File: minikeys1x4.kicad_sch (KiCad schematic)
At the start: 15 parts

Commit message: add placeholder keys, xtals, LED, debug
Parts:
- added C? (x2): DNP, symbol Device:C_Small
- added C? (x2): ?, symbol Device:C_Small
- added D?: LED_Small, symbol Device:LED_Small
- added R? (x2): ?, symbol Device:R_Small_US
- added R?: 0, symbol Device:R_Small_US
- added SW? (x4): SW_Push_45deg, symbol Switch:SW_Push_45deg
- added Y?: 32kHz, symbol Device:Crystal_GND24_Small
- added Y?: 8MHz, symbol Device:Crystal_GND24_Small
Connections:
- net +3V3: now also SW?.1, SW?.1, SW?.1, SW?.1
- net GND: now also C?.2, C?.2, C?.2, C?.2, R?.2, Y?.2 (G), Y?.2 (G), Y?.4 (G), Y?.4 (G)
- net nRST: now also C?.1; no longer R?.2, SW?.1
- net KEY_0: now reaches U?.11 (PA1)
- net KEY_0: now also SW?.2
- net KEY_1: now reaches U?.12 (PA2)
- net KEY_1: now also SW?.2
- net KEY_2: now reaches U?.13 (PA3)
- net KEY_2: now also SW?.2
- net KEY_3: now reaches U?.14 (PA4)
- net KEY_3: now also SW?.2
- net LED_0: now reaches U?.16 (PA6)
- net LED_0: now also D?.2 (A)
- net LSE_IN: now reaches U?.3 (PC14)
- net LSE_IN: now also C?.1, Y?.3
- net USBD_N: now reaches U?.32 (PA11)
- net USBD_P: now reaches U?.33 (PA12)
- net SWDIO: now reaches U?.34 (PA13)
- net SWCLK: now reaches U?.37 (PA14)
- net JTDI: now reaches U?.38 (PA15)
- net JTDO: now reaches U?.39 (PB3)
- net LSE_OUT: now reaches U?.4 (PC15)
- net LSE_OUT: now also R?.1
- net NJTRST: now reaches U?.40 (PB4)
- net HSE_IN: now reaches U?.5 (PD0)
- net HSE_IN: now also C?.1, Y?.3
- net HSE_OUT: now reaches U?.6 (PD1)
- net HSE_OUT: now also R?.1
- new net: R?.2, SW?.1
- new net: C?.1, R?.2, Y?.1 (x2)
- new net: D?.1 (K), R?.1
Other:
- note added: "TIM3_CH1"
- note added: "should this LED low side drive?"
- moved on the sheet: C?, J?, R?, SW?, U?

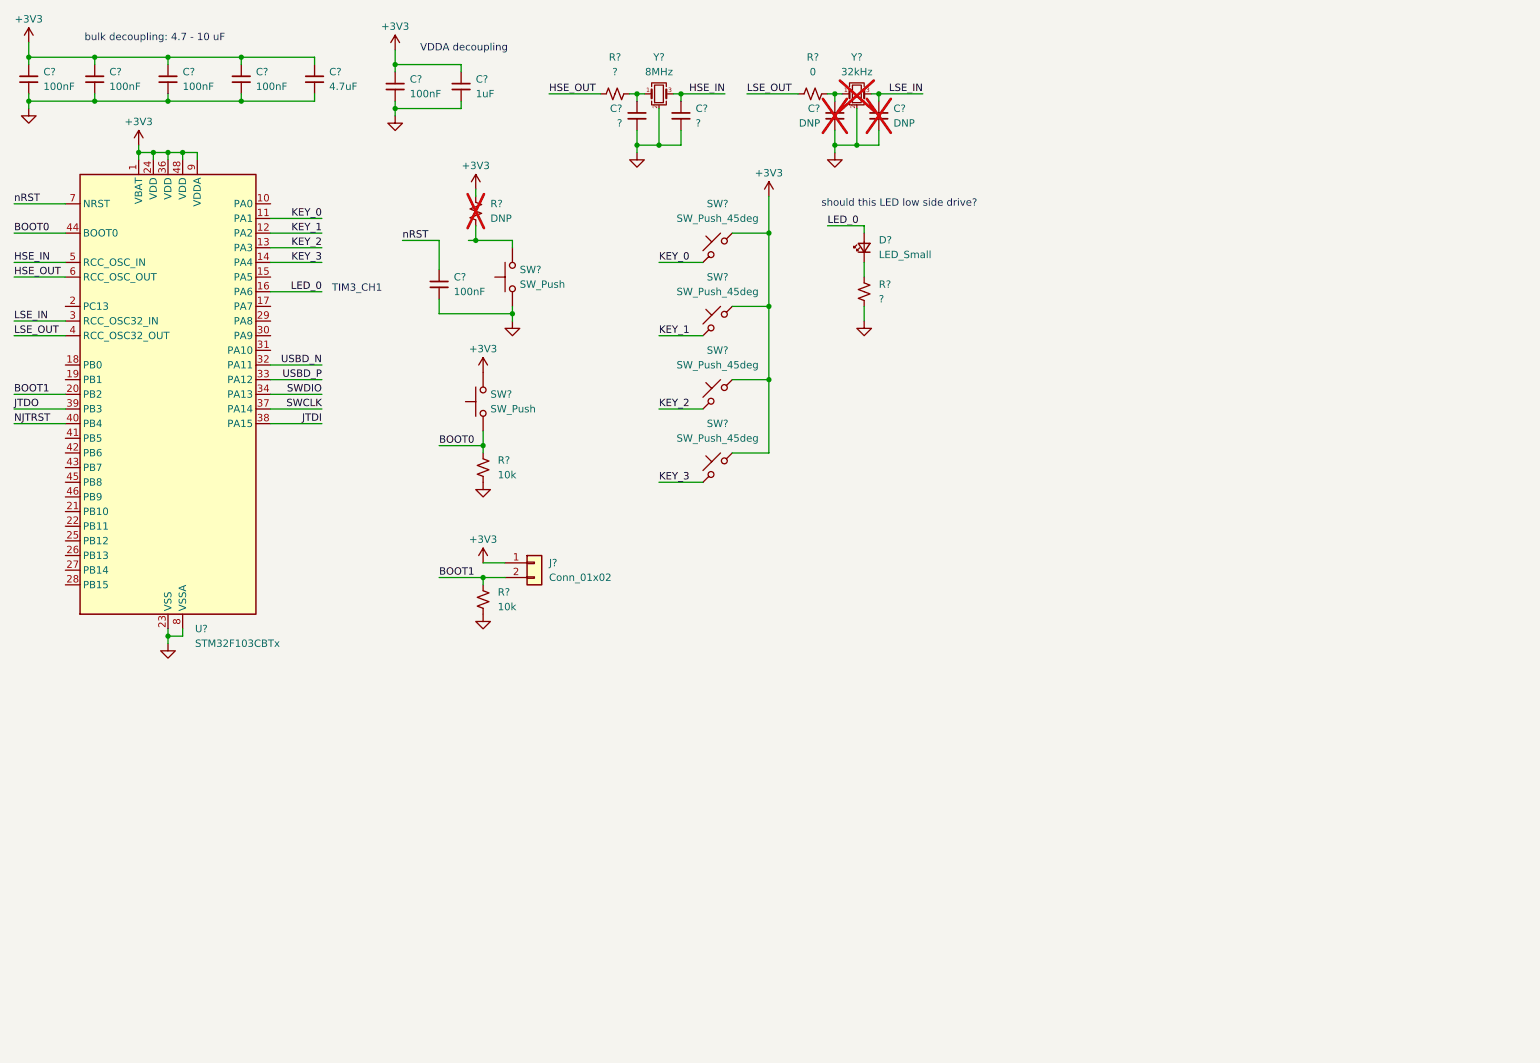
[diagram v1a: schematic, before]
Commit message: add project footprint and USB
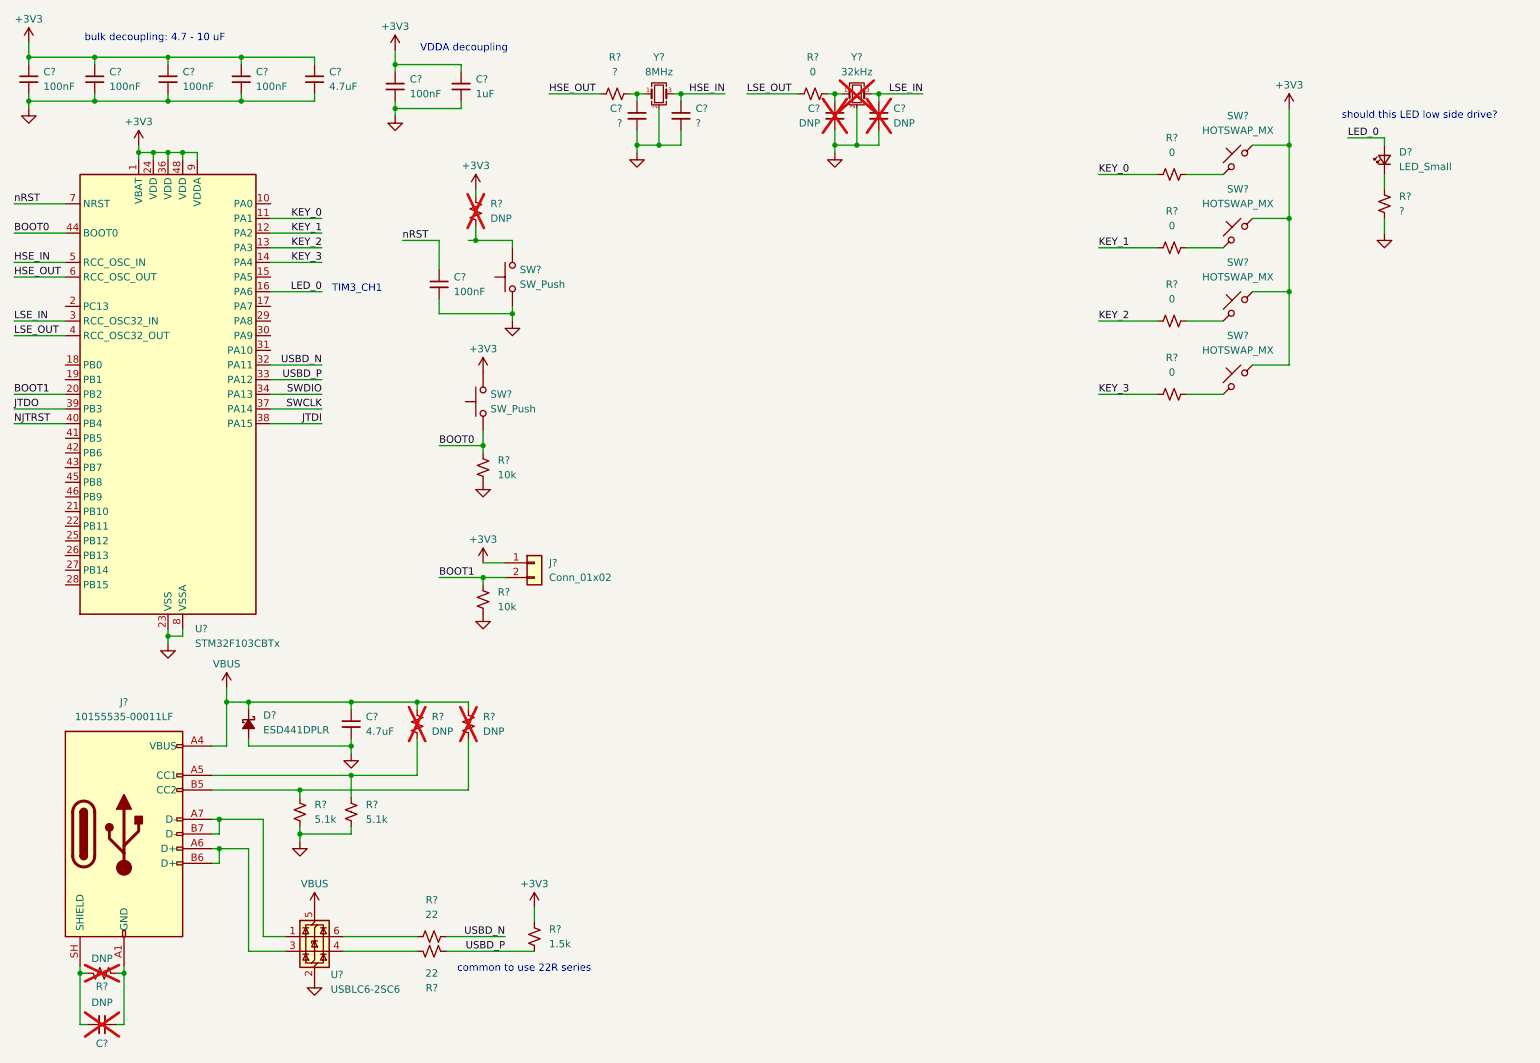
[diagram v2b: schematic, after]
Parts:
- added C?: DNP, symbol Device:C_Small
- added C?: 4.7uF, symbol Device:C_Small
- added D?: ESD441DPLR, symbol Device:D_Schottky_Small_Filled
- added J?: 10155535-00011LF, symbol Connector:USB_C_Receptacle_USB2.0_14P
- added R?: 1.5k, symbol Device:R_Small_US
- added R? (x2): 22, symbol Device:R_Small_US
- added R? (x3): DNP, symbol Device:R_Small_US
- added R? (x2): 5.1k, symbol Device:R_Small_US
- added R? (x4): 0, symbol Device:R_Small_US
- added U?: USBLC6-2SC6, Package_TO_SOT_SMD:SOT-23-6, symbol Power_Protection:USBLC6-2SC6
- SW? (x4): value SW_Push_45deg -> HOTSWAP_MX; footprint (none) -> minikeys_footprints:Kailh_socket_MX_optional_reversible_platemount
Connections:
- net +3V3: now also R?.1
- net GND: now also C?.2, D?.2 (A), R?.2, R?.2, U?.2 (GND)
- net KEY_0: now also R?.1; no longer SW?.2
- net KEY_1: now also R?.1; no longer SW?.2
- net KEY_2: now also R?.1; no longer SW?.2
- net KEY_3: now also R?.1; no longer SW?.2
- net USBD_N: now also R?.2
- net USBD_P: now also R?.2, R?.2
- new net: R?.1, U?.6 (I/O1)
- new net: C?.1, J?.SH (SHIELD), R?.1
- new net: C?.2, J?.A1 (GND), J?.A12 (GND), J?.B1 (GND), J?.B12 (GND), R?.2
- new net: J?.A5 (CC1), R?.1, R?.2
- new net: R?.2, SW?.2 (x4)
- new net: R?.1, U?.4 (I/O2)
- new net: J?.B5 (CC2), R?.1, R?.2
- new net: J?.A6 (D+), J?.B6 (D+), U?.3 (I/O2)
- new net: J?.A7 (D-), J?.B7 (D-), U?.1 (I/O1)
- new net VBUS: C?.1, D?.1 (K), J?.A4 (VBUS), J?.A9 (VBUS), J?.B4 (VBUS), J?.B9 (VBUS), R?.1, R?.1, U?.5 (VBUS)
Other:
- note added: "common to use 22R series"
- moved on the sheet: D?, R?, SW?
